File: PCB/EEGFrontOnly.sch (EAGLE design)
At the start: 36 parts, among them IC1 ADS1299-X, J2 USB_B_PTH, U1 LP2985-33DBVT, U2 B0505S-1WB0505S-1W, U3 TPS60403DBVT, U4 TPS73225DBVR, U5 TPS73225DBVR

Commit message: ads stuff init
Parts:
- added C21, C23, C25, C30, C31, C32, C34: 1.0uF, SparkFun-Capacitors:1.0UF-0402-16V-10%
- added C22, C24, C26, C27, C33, C35: 0.1uF, SparkFun-Capacitors:0.1UF-0402-16V-10%
- added C28: 10uF, SparkFun-Capacitors:10UF-0402-6.3V-20%
- added C29: 100uF, jingjieparts:100UF-1210-20%-10V
- added C36, C37: NI, SparkFun-Capacitors:0.1UF-0402-16V-10%
- added J5: (no value), SparkFun-Connectors:CONN_02
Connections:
- new net N$10: C27.2, C28.2, IC1.VREFP
- new net N$11: IC1.SRB2, J5.1
- new net N$12: IC1.SRB1, J5.2
- new net VCAP1: C29.1, IC1.VCAP1
- new net VCAP2: C30.1, IC1.VCAP2
- new net VCAP3: C31.1, C33.1, IC1.VCAP3
- new net VCAP4: C32.2, IC1.VCAP4
- net AGND: now also C21.2, C22.2, C23.2, C24.2, C25.2, C26.2, C34.2, C35.2
- net AVDD: now also C21.1, C22.1, C36.1, C37.1, IC1.AVDD1, IC1.AVDD_1, IC1.AVDD_2, IC1.AVDD_3, IC1.AVDD_4, IC1.AVDD_5
- net AVSS: now also C23.1, C24.1, C27.1, C28.1, C29.2, C30.2, C31.2, C32.1, C33.2, C34.1, C35.1, C36.2, C37.2, IC1.AVSS1, IC1.AVSS_1, IC1.AVSS_2, IC1.AVSS_3, IC1.AVSS_4, IC1.AVSS_5, IC1.VREFN
- net DGND: now also IC1.DGND_1, IC1.DGND_2, IC1.DGND_3
- net DVDD: now also C25.1, C26.1, IC1.DVDD_1, IC1.DVDD_2

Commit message: STUFF
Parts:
- added C38: 1.5nF, SparkFun-Capacitors:1.5NF-0402
- added C39, C40, C41, C42, C43, C44, C45, C46, C47, C48: 4.7nF, SparkFun-Capacitors:4.7NF-0402
- added R10, R11, R12, R13, R4, R5, R6, R7, R8, R9: 4.99K, SparkFun-Resistors:4.99KOHM-0402
- added R3: 1M, SparkFun-Resistors:1MOHM-0402-1/4W-5%
- added U6, U7, U8: TPD4E1B06DCKR, jingjieparts:TPD4E1B06DCKR
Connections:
- new net N$13: C38.2, IC1.BIASINV, R3.1
- new net N$14: C38.1, C39.1, IC1.BIASIN, IC1.BIASOUT, R3.2, R4.2
- new net N$15: C40.1, IC1.IN8P, R5.2
- new net N$16: C41.1, IC1.IN7P, R6.2
- new net N$17: C42.1, IC1.IN6P, R7.2
- new net N$18: C43.1, IC1.IN5P, R8.2
- new net N$19: C44.1, IC1.IN4P, R9.2
- new net N$20: C45.1, IC1.IN3P, R10.2
- new net N$21: C46.1, IC1.IN2P, R11.2
- new net N$22: C47.1, IC1.IN1P, R12.2
- new net P_BIAS: R4.1, U6.IO1
- new net P_IN1: R12.1, U8.IO1
- new net P_IN2: R11.1, U7.IO3
- new net P_IN3: R10.1, U7.IO4
- new net P_IN4: R9.1, U7.IO2
- new net P_IN5: R8.1, U7.IO1
- new net P_IN6: R7.1, U6.IO3
- new net P_IN7: R6.1, U6.IO4
- new net P_IN8: R5.1, U6.IO2
- new net P_REF: R13.1, U8.IO2
- net AGND: now also C39.2, C40.2, C41.2, C42.2, C43.2, C44.2, C45.2, C46.2, C47.2, C48.2, U6.GND, U7.GND, U8.GND
- net DGND: now also IC1.RESV1
- net N$12: now also C48.1, R13.2
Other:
- moved on the sheet: C27, C28, C29, C30, C31, C32, C33, IC1, J5

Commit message: partly complete the ADS part
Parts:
- added IC2: ADUM3151-3, analog-devices-adum315x:ADUM3151-3
- added J6, J7: (no value), SparkFun-Connectors:CONN_10"
- added R14, R15, R16: 10k, SparkFun-Resistors:10KOHM-0402-1/10W-1%
- added R17, R18, R19, R20: 22, SparkFun-Resistors:22OHM-0402-1/10W-1%
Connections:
- new net CLK_NC: IC1.CLK
- new net N$23: IC1.DOUT, R17.1
- new net N$24: IC1.SCLK, R18.1
- new net N$25: IC1.!CS, R19.1
- new net N$26: IC1.DIN, R20.1
- new net PWD: IC1.!PWDN, J7.3, R16.1
- new net RST: IC1.!RESET, J7.4, R15.1
- new net SPI_CLK: J7.7, R18.2
- new net SPI_CS: J7.6, R14.1, R19.2
- new net SPI_DRDY: IC1.!DRDY, J7.9
- new net SPI_MISO: J7.8, R17.2
- new net SPI_MOSI: J7.2, R20.2
- new net SPI_START: IC1.START, J7.5
- net AGND: now also U6.NC, U7.NC, U8.NC; no longer C25.2, C26.2
- net DGND: now also C25.2, C26.2, IC1.DAISY_IN, J7.1
- net DVDD: now also IC1.CLKSEL, J7.10, R14.2, R15.2, R16.2
- net P_BIAS: now also J6.10
- net P_IN1: now also J6.2
- net P_IN2: now also J6.3
- net P_IN3: now also J6.4
- net P_IN4: now also J6.5
- net P_IN5: now also J6.6
- net P_IN6: now also J6.7
- net P_IN7: now also J6.8
- net P_IN8: now also J6.9
- net P_REF: now also J6.1

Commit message: SPI_ISO
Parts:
- added C49, C50: 10uF, SparkFun-Capacitors:10UF-0603-6.3V-20%
- added C51, C52: 22nF, SparkFun-Capacitors:22NF/22,000PF-0402-50V-10%
- added IC3: HT7333, holtek2:HT7333
- added J8: (no value), SparkFun-Connectors:CONN_10"
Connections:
- new net SPI_ISO_CLK: IC2.MCLK, J8.9
- new net SPI_ISO_CS: IC2.!MSS, J8.6
- new net SPI_ISO_DRDY: IC2.VOC, J8.3
- new net SPI_ISO_MISO: IC2.MI, J8.7
- new net SPI_ISO_MOSI: IC2.MO, J8.8
- new net SPI_ISO_RST: IC2.VIB, J8.4
- new net SPI_ISO_START: IC2.VIA, J8.5
- new net SPI_PWD: J8.2
- new net VCCIO: C50.1, C51.1, IC2.VDD1, IC3.OUT, J8.10
- net DGND: now also C52.2, IC2.GND2
- net DVDD: now also C52.1, IC2.VDD2
- net GND-ISO: now also C49.2, C50.2, C51.2, IC2.GND1, IC3.GND, J8.1
- net RST: now also IC2.VOB
- net SPI_CLK: now also IC2.SCLK
- net SPI_CS: now also IC2.!SSS
- net SPI_DRDY: now also IC2.VIC
- net SPI_MISO: now also IC2.SO
- net SPI_MOSI: now also IC2.SI
- net SPI_START: now also IC2.VOA
- net VCC-ISO: now also C49.1, IC3.IN
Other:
- moved on the sheet: J6, J7, U6, U7, U8

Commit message: PCB wiring complete
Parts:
- added C53, C54: 0.1uF, SparkFun-Capacitors:0.1UF-0402-16V-10%
- added S1: MOMENTARY-SWITCH-SPST-PTH-6.0MM, SparkFun-Switches:MOMENTARY-SWITCH-SPST-PTH-6.0MM
- added U10: ISO721D, Texas Instruments_By_element14_Batch_1:ISO721D
- J2: value USB_B_PTH -> (none); device SparkFun-Connectors:USB_B_PTH -> SparkFun-Connectors:USB_MICRO-BREDUCED_PASTE
- renumbered IC3 to U9
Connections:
- removed net SPI_PWD: J8.2
- new net ISO_PWD: J8.2, U10.OUT
- net DGND: now also C53.2, S1.1, U10.GND1
- net DVDD: now also C53.1, U10.VCC1, U10.VCC1_2
- net GND-ISO: now also C54.2, U10.GND2, U10.GND2_2
- net PWD: now also U10.IN
- net RST: now also S1.2
- net VCCIO: now also C54.1, U10.VCC2

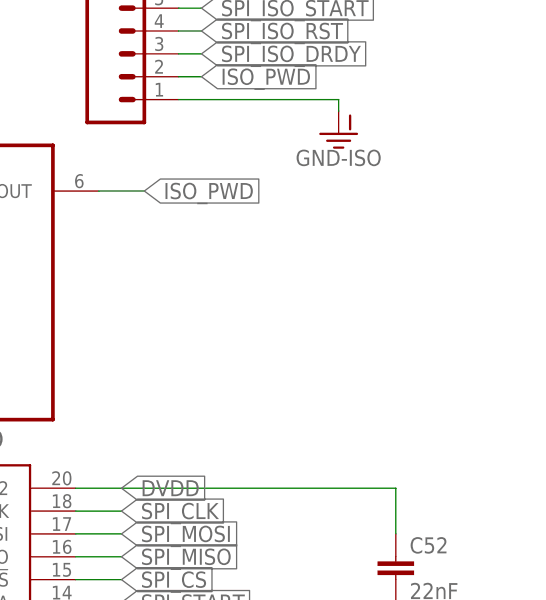
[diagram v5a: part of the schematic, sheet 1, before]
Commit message: text adjusting & add power pins and less
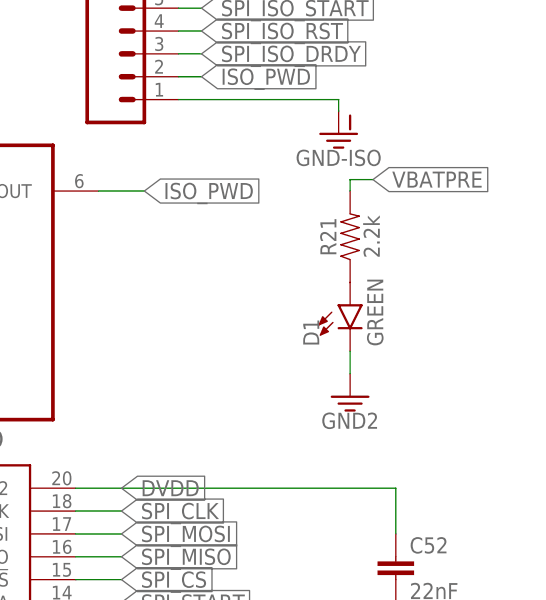
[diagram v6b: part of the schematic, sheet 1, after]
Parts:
- added D1: GREEN, SparkFun-LED:LED-GREEN0603
- added J9: (no value), SparkFun-Connectors:CONN_06SILK_FEMALE_PTH
- added R21: 2.2k, SparkFun-Resistors:2.2KOHM-0603-1/10W-1%
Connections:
- new net N$27: D1.A, R21.1
- net AGND: now also J9.1
- net AVDD: now also J9.3
- net AVSS: now also J9.4
- net DGND: now also J9.6
- net DVDD: now also J9.5
- net GND: now also D1.C
- net VBAT: now also J9.2
- net VBATPRE: now also R21.2
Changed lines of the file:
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@@
 <setting verticaltext="up"/>
 </settings>
-<grid distance="0.025" unitdist="inch" unit="inch" style="lines" multiple="1" display="no" altdistance="0.01" altunitdist="inch" altunit="inch"/>
+<grid distance="0.05" unitdist="inch" unit="inch" style="lines" multiple="1" display="no" altdistance="0.01" altunitdist="inch" altunit="inch"/>
 <layers>
 <layer number="1" name="Top" color="4" fill="1" visible="no" active="no"/>
@@
 <part name="J2" library="SparkFun-Connectors" deviceset="USB_MICRO-B" device="REDUCED_PASTE"/>
 <part name="SUPPLY10" library="supply2" library_urn="urn:adsk.eagle:library:372" deviceset="DGND" device=""/>
+<part name="D1" library="SparkFun-LED" deviceset="LED-GREEN" device="0603" value="GREEN"/>
+<part name="R21" library="SparkFun-Resistors" deviceset="2.2KOHM" device="-0603-1/10W-1%" value="2.2k"/>
+<part name="GND5" library="SparkFun-PowerSymbols" deviceset="GND2" device=""/>
+<part name="J9" library="SparkFun-Connectors" deviceset="CONN_06" device="SILK_FEMALE_PTH"/>
 </parts>
 <sheets>
@@
 <instance part="C54" gate="G$1" x="168.91" y="71.12"/>
 <instance part="J2" gate="G$1" x="233.045" y="135.89"/>
+<instance part="D1" gate="G$1" x="254" y="71.12"/>
+<instance part="R21" gate="G$1" x="254" y="78.74" rot="R90"/>
+<instance part="GND5" gate="G$1" x="254" y="60.96"/>
 </instances>
 <busses>
@@
 <wire x1="212.09" y1="153.67" x2="217.17" y2="153.67" width="0.1524" layer="91"/>
 <label x="217.17" y="153.67" size="1.778" layer="95" xref="yes"/>
+</segment>
+<segment>
+<pinref part="D1" gate="G$1" pin="C"/>
+<pinref part="GND5" gate="G$1" pin="3.3V"/>
+<wire x1="254" y1="63.5" x2="254" y2="66.04" width="0.1524" layer="91"/>
 </segment>
 </net>
@@
 <label x="217.17" y="151.13" size="1.778" layer="95" xref="yes"/>
 </segment>
+<segment>
+<pinref part="R21" gate="G$1" pin="2"/>
+<wire x1="254" y1="83.82" x2="254" y2="85.09" width="0.1524" layer="91"/>
+<wire x1="254" y1="85.09" x2="256.54" y2="85.09" width="0.1524" layer="91"/>
+<label x="256.54" y="85.09" size="1.778" layer="95" xref="yes"/>
+</segment>
 </net>
 <net name="N$3" class="0">
@@
 <wire x1="226.06" y1="83.82" x2="231.14" y2="83.82" width="0.1524" layer="91"/>
 <label x="231.14" y="83.82" size="1.778" layer="95" xref="yes"/>
+</segment>
+</net>
+<net name="N$27" class="0">
+<segment>
+<pinref part="R21" gate="G$1" pin="1"/>
+<pinref part="D1" gate="G$1" pin="A"/>
 </segment>
 </net>
@@
 <instance part="S1" gate="G$1" x="88.9" y="22.86"/>
 <instance part="SUPPLY10" gate="G$1" x="75.565" y="19.05"/>
+<instance part="J9" gate="G$1" x="125.73" y="26.67"/>
 </instances>
 <busses>
@@
 <wire x1="245.11" y1="125.73" x2="245.11" y2="127" width="0.1524" layer="91"/>
 <label x="245.11" y="127" size="1.778" layer="95" xref="yes"/>
+</segment>
+<segment>
+<pinref part="J9" gate="G$1" pin="3"/>
+<wire x1="130.81" y1="26.67" x2="132.08" y2="26.67" width="0.1524" layer="91"/>
+<label x="132.08" y="26.67" size="1.778" layer="95" xref="yes"/>
 </segment>
 </net>
@@
 <label x="245.11" y="116.84" size="1.778" layer="95" xref="yes"/>
 </segment>
+<segment>
+<pinref part="J9" gate="G$1" pin="4"/>
+<wire x1="130.81" y1="29.21" x2="132.08" y2="29.21" width="0.1524" layer="91"/>
+<label x="132.08" y="29.21" size="1.778" layer="95" xref="yes"/>
+</segment>
 </net>
 <net name="DVDD" class="0">
@@
 <junction x="198.12" y="110.49"/>
 <label x="201.93" y="110.49" size="1.778" layer="95" xref="yes"/>
+</segment>
+<segment>
+<pinref part="J9" gate="G$1" pin="5"/>
+<wire x1="130.81" y1="31.75" x2="132.08" y2="31.75" width="0.1524" layer="91"/>
+<label x="132.08" y="31.75" size="1.778" layer="95" xref="yes"/>
 </segment>
 </net>
@@
 <wire x1="83.82" y1="22.86" x2="75.565" y2="22.86" width="0.1524" layer="91"/>
 <wire x1="75.565" y1="22.86" x2="75.565" y2="21.59" width="0.1524" layer="91"/>
+</segment>
+<segment>
+<pinref part="J9" gate="G$1" pin="6"/>
+<wire x1="130.81" y1="34.29" x2="132.08" y2="34.29" width="0.1524" layer="91"/>
+<label x="132.08" y="34.29" size="1.778" layer="95" xref="yes"/>
 </segment>
 </net>
@@
 <wire x1="262.89" y1="86.36" x2="248.92" y2="86.36" width="0.1524" layer="91"/>
 </segment>
+<segment>
+<pinref part="J9" gate="G$1" pin="1"/>
+<wire x1="130.81" y1="21.59" x2="132.08" y2="21.59" width="0.1524" layer="91"/>
+<label x="132.08" y="21.59" size="1.778" layer="95" xref="yes"/>
+</segment>
 </net>
 <net name="N$10" class="0">
@@
 </segment>
 </net>
+<net name="VBAT" class="0">
+<segment>
+<pinref part="J9" gate="G$1" pin="2"/>
+<wire x1="130.81" y1="24.13" x2="132.08" y2="24.13" width="0.1524" layer="91"/>
+<label x="132.08" y="24.13" size="1.778" layer="95" xref="yes"/>
+</segment>
+</net>

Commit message: front only PCB complete!
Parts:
- added J10: (no value), SparkFun-Connectors:CONN_02
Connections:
- net P_BIAS: now also J10.2
- net P_IN8: now also J10.1
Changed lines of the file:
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@@
 <setting verticaltext="up"/>
 </settings>
-<grid distance="0.05" unitdist="inch" unit="inch" style="lines" multiple="1" display="no" altdistance="0.01" altunitdist="inch" altunit="inch"/>
+<grid distance="0.1" unitdist="inch" unit="inch" style="lines" multiple="1" display="no" altdistance="0.01" altunitdist="inch" altunit="inch"/>
 <layers>
 <layer number="1" name="Top" color="4" fill="1" visible="no" active="no"/>
@@
 <part name="GND5" library="SparkFun-PowerSymbols" deviceset="GND2" device=""/>
 <part name="J9" library="SparkFun-Connectors" deviceset="CONN_06" device="SILK_FEMALE_PTH"/>
+<part name="J10" library="SparkFun-Connectors" deviceset="CONN_02" device=""/>
 </parts>
 <sheets>
@@
 <instance part="SUPPLY10" gate="G$1" x="75.565" y="19.05"/>
 <instance part="J9" gate="G$1" x="125.73" y="26.67"/>
+<instance part="J10" gate="G$1" x="7.62" y="165.1"/>
 </instances>
 <busses>
@@
 <label x="218.44" y="81.28" size="1.778" layer="95" rot="R180" xref="yes"/>
 </segment>
+<segment>
+<pinref part="J10" gate="G$1" pin="1"/>
+<wire x1="15.24" y1="165.1" x2="17.78" y2="165.1" width="0.1524" layer="91"/>
+<label x="17.78" y="165.1" size="1.778" layer="95" xref="yes"/>
+</segment>
 </net>
 <net name="P_BIAS" class="0">
@@
 <label x="218.44" y="86.36" size="1.778" layer="95" rot="R180" xref="yes"/>
 </segment>
-</net>
+<segment>
+<pinref part="J10" gate="G$1" pin="2"/>
+<wire x1="15.24" y1="167.64" x2="17.78" y2="167.64" width="0.1524" layer="91"/>
+<label x="17.78" y="167.64" size="1.778" layer="95" xref="yes"/>
+</segment>
+</net>
